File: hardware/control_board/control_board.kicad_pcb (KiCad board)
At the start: 2 copper layers, 101.6 x 53.3 mm, 38 parts, among them J1 PWR_SWITCHES, J10 MO2_SW_FW, J11 MO3_SW_FW, J12 MO0_SW_BW, J13 MO1_SW_BW, J14 MO2_SW_BW, J15 MO3_SW_BW, J2 UI_SWITCHES, J3 ATX-24, J4 MOT0, J5 MOT1, J6 MOT2, J7 MOT3, J8 MO0_SW_FW, J9 MO1_SW_FW, P1 Digital, P2 Power, P3 Analog, P4 Analog, P5 PWM, P6 PWM, P7 Communication, Q1 BSS138

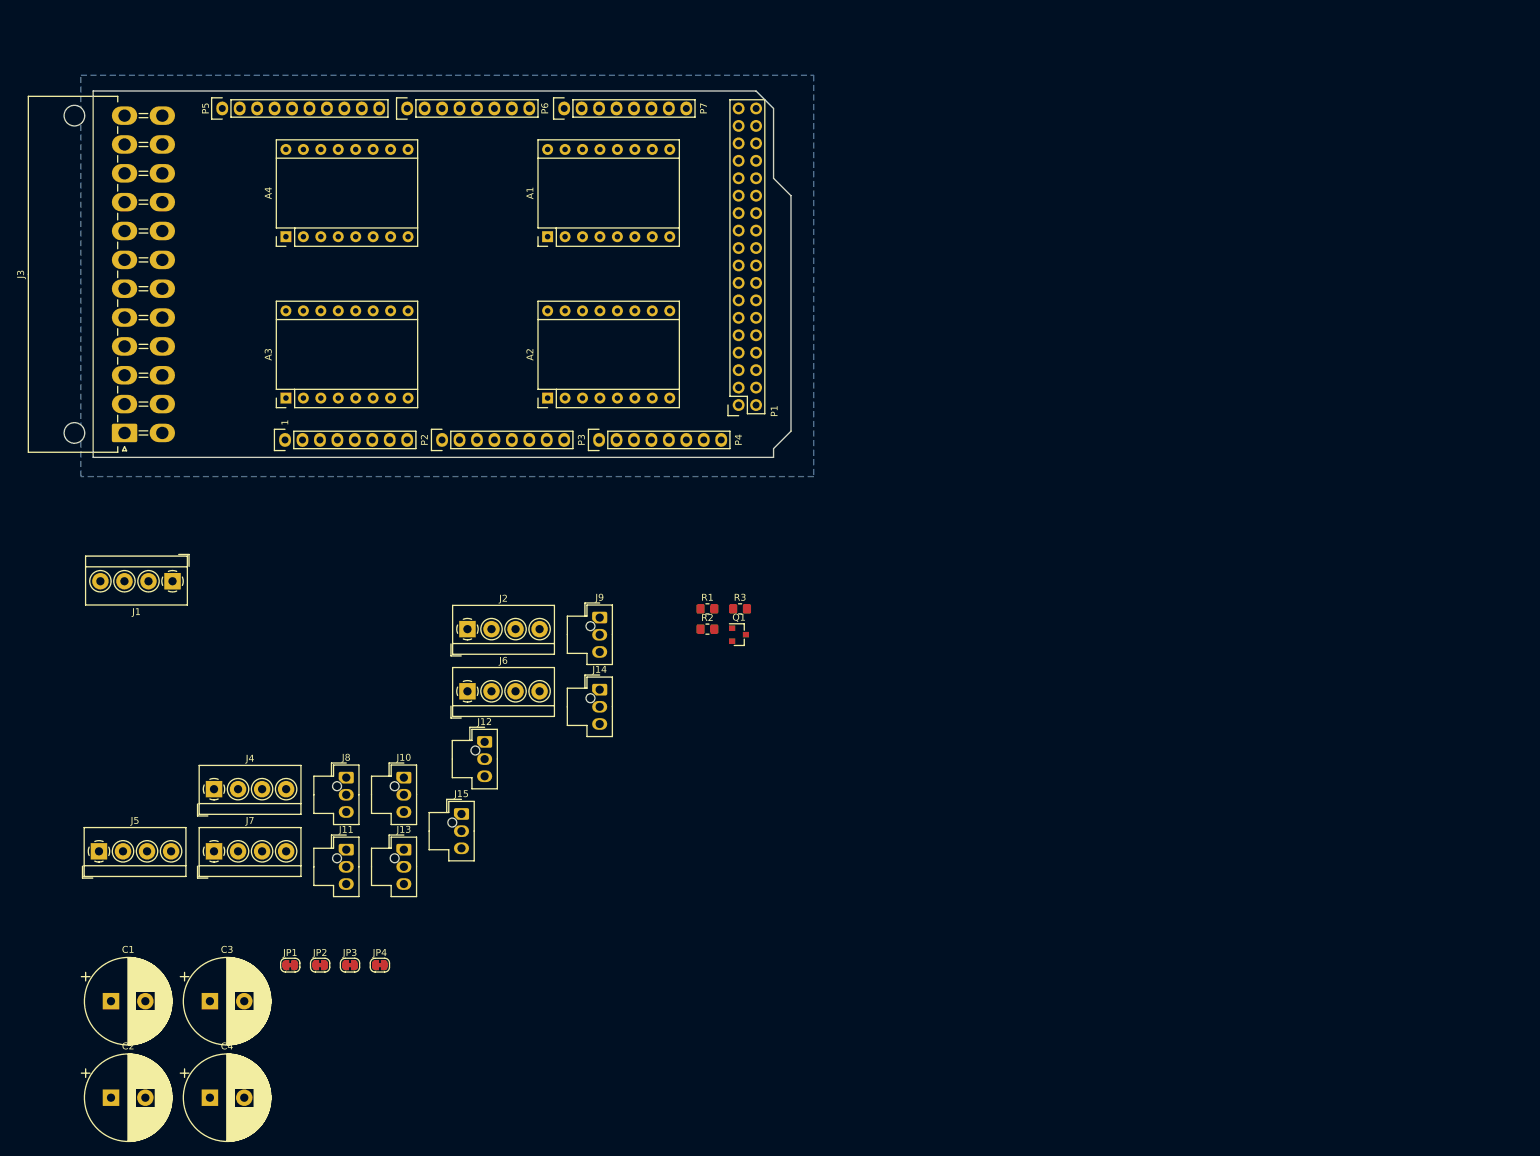
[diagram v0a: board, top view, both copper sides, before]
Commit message: add ps on led
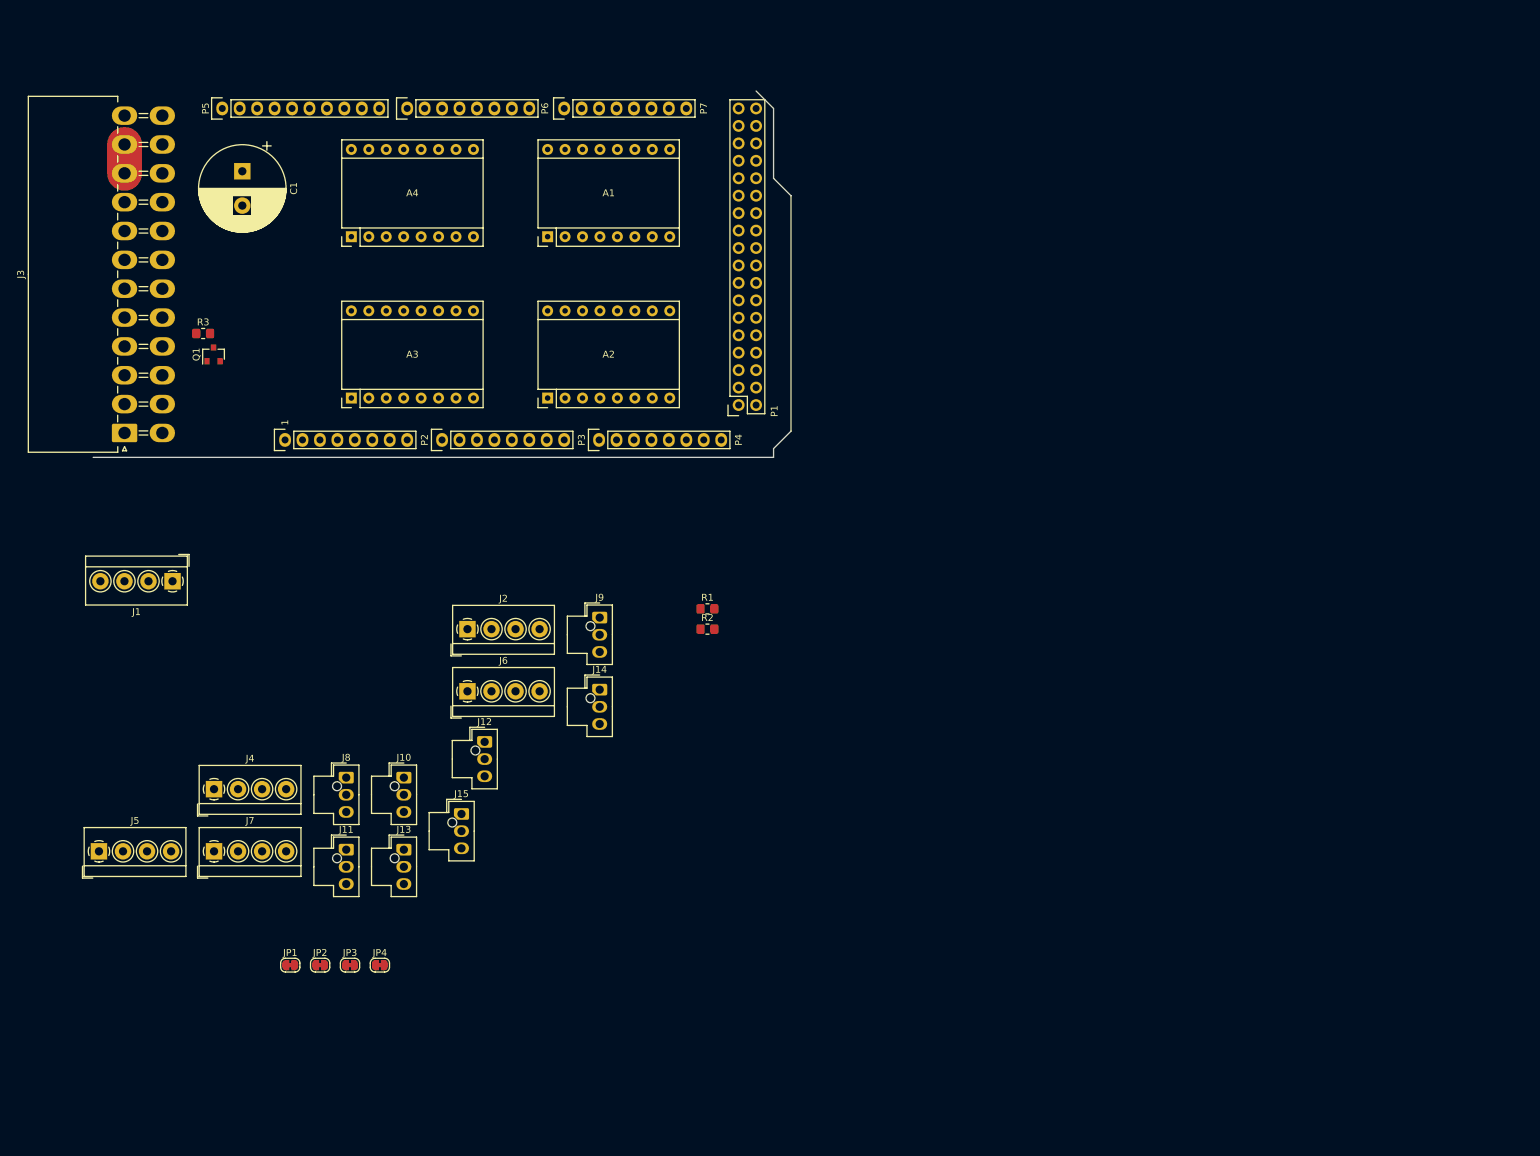
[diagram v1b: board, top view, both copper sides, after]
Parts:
- removed C2, C3, C4: 100uF, Capacitor_THT:CP_Radial_D12.5mm_P5.00mm
- moved C1 122.3 mm to (125.1, 80.0), turned to 270 degrees
- moved R3 87.9 mm to (119.4, 103.6)
- moved Q1 86.7 mm to (120.9, 106.7), turned to 90 degrees
- moved A3 9.53 mm to (141.0, 113.0)
- moved A4 9.53 mm to (141.0, 89.5)
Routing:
- net +12V: track 0.00 -> 4.20 mm
- added copper zone on In1.Cu, net PWR_SW_L
- removed copper zone on B.Cu, net PWR_SW_L
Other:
- outline, holes or cut-outs redrawn
- copper layers 2 -> 4
- rule trace_min: 0.2 -> 0.1524

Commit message: add misc connectors
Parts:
- added D1: PS_ON, LED_SMD:LED_0805_2012Metric_Pad1.15x1.40mm_HandSolder, F.Cu at (305.7, 108.7)
- added J16: MISC_SIG, TerminalBlock_4Ucon:TerminalBlock_4Ucon_1x04_P3.50mm_Horizontal, F.Cu at (232.7, 138.8)
- added J17: MISC_PWR, TerminalBlock_4Ucon:TerminalBlock_4Ucon_1x04_P3.50mm_Horizontal, F.Cu at (249.5, 129.7)
- added R4: R_200, Resistor_SMD:R_0805_2012Metric_Pad1.20x1.40mm_HandSolder, F.Cu at (310.4, 111.7)
- moved J13 160.8 mm to (293.9, 109.9)
- moved J7 160.1 mm to (266.2, 111.6)
- moved J4 141.2 mm to (249.5, 111.6)
- moved J11 137.7 mm to (268.7, 129.5)
- moved J8 137.7 mm to (268.7, 119.0)
- moved J5 137.7 mm to (232.7, 129.7)
- moved C1 133.8 mm to (234.5, 157.0), turned to 0 degrees
- moved J15 127.5 mm to (277.1, 130.9)
- moved J12 124.3 mm to (277.1, 120.4)
- moved R2 123.6 mm to (310.4, 108.7)
- moved JP1 122.3 mm to (246.2, 151.7)
- moved J1 121.1 mm to (232.7, 111.6), turned to 0 degrees
- moved JP3 118.2 mm to (250.5, 151.7)
- moved R1 117.3 mm to (305.6, 111.7)
- moved JP2 116.9 mm to (246.2, 155.3)
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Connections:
- P1 pad 10: /Arduino Shield Connections/47 -> MISC_1
- P1 pad 7: /Arduino Shield Connections/48 -> MISC_2
- P1 pad 8: /Arduino Shield Connections/49 -> MISC_3
- P1 pad 9: /Arduino Shield Connections/46 -> MISC_0
- P5 pad 5: /Arduino Shield Connections/13(**) -> UI_SWITCH_1
- P5 pad 6: /Arduino Shield Connections/12(**) -> UI_SWITCH_0

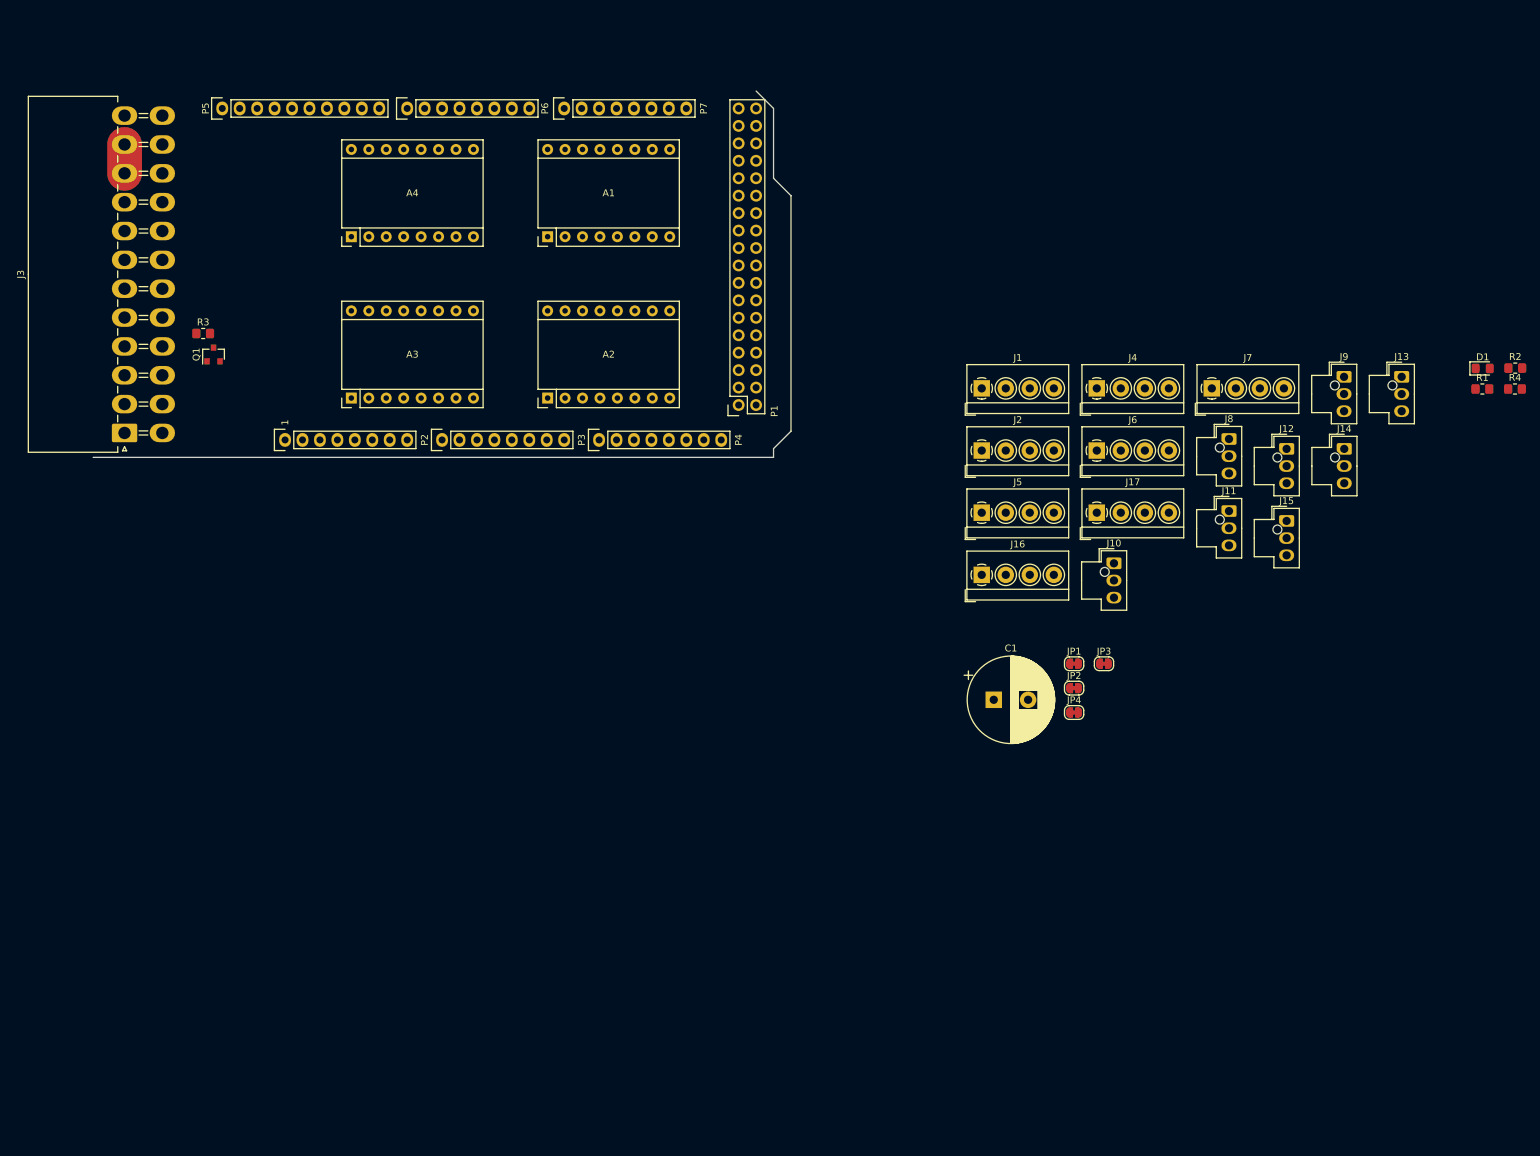
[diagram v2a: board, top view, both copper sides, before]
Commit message: finish layout, add fusing
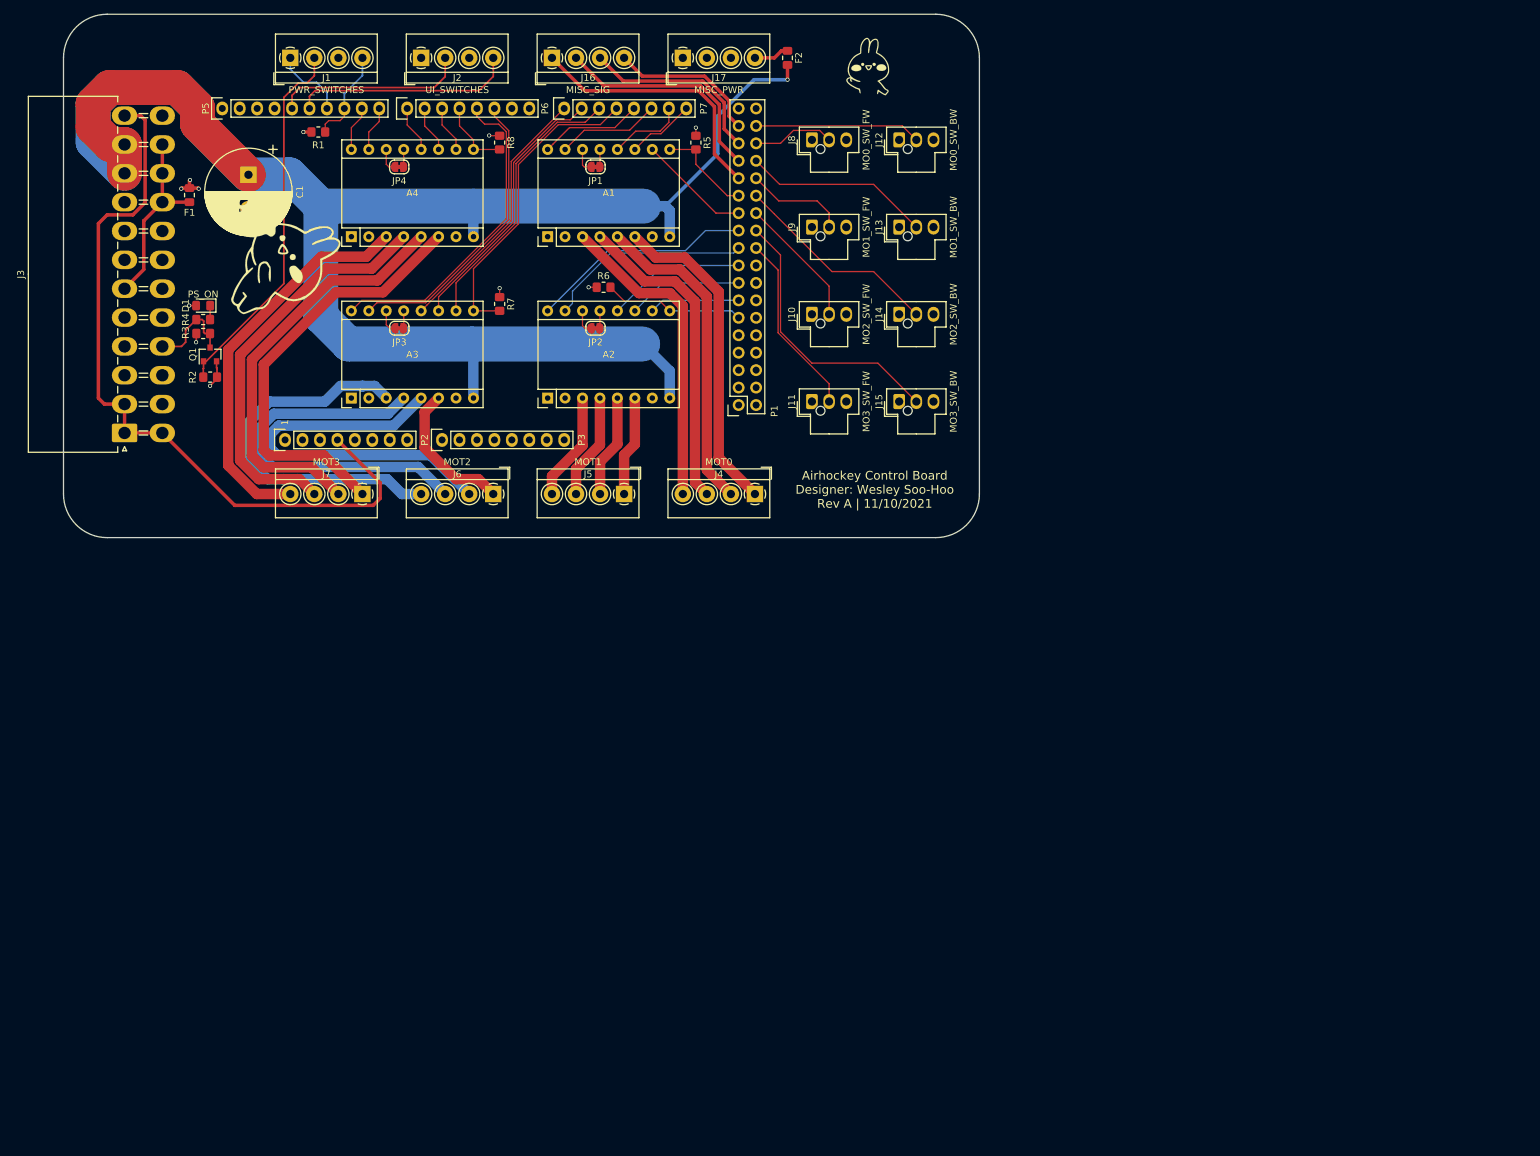
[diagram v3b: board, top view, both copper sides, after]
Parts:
- removed P4: Analog, Socket_Arduino_Mega:Socket_Strip_Arduino_1x08
- added F1: 1A, Fuse:Fuse_0805_2012Metric_Pad1.15x1.40mm_HandSolder, F.Cu at (117.4, 83.5)
- added F2: 1A, Fuse:Fuse_0805_2012Metric_Pad1.15x1.40mm_HandSolder, F.Cu at (204.5, 63.5)
- added G***: LOGO, img:mimi_doll, B.Cu at (188.0, 94.0)
- added G***: LOGO, img:mimi_heart, F.Cu at (128.9, 91.4)
- added G***: LOGO, img:mimi, F.Cu at (216.5, 64.1)
- added G***: LOGO, img:mimi_melon, B.Cu at (132.1, 111.8)
- added R5: R_10K, Resistor_SMD:R_0805_2012Metric_Pad1.20x1.40mm_HandSolder, F.Cu at (191.1, 75.8)
- added R6: R_10K, Resistor_SMD:R_0805_2012Metric_Pad1.20x1.40mm_HandSolder, F.Cu at (177.7, 96.9)
- added R7: R_10K, Resistor_SMD:R_0805_2012Metric_Pad1.20x1.40mm_HandSolder, F.Cu at (162.6, 99.3)
- added R8: R_10K, Resistor_SMD:R_0805_2012Metric_Pad1.20x1.40mm_HandSolder, F.Cu at (162.6, 75.8)
- moved R4 191.3 mm to (119.4, 101.6), turned to 180 degrees
- moved R2 190.0 mm to (120.4, 110.0)
- moved D1 186.5 mm to (119.4, 99.6), turned to 180 degrees
- moved R1 173.6 mm to (136.2, 74.3)
- moved C1 132.7 mm to (126.0, 80.5), turned to 270 degrees
- moved JP4 126.4 mm to (147.9, 79.4)
- moved J7 124.6 mm to (142.6, 127.0), turned to 180 degrees
- moved JP3 113.6 mm to (148.0, 102.9)
- moved J1 111.6 mm to (132.1, 63.5)
- moved JP1 100.4 mm to (176.5, 79.4)
- moved J2 99.7 mm to (151.1, 63.5)
- moved J16 97.9 mm to (170.2, 63.5)
- moved J17 89.5 mm to (189.2, 63.5)
- moved J6 88.1 mm to (161.6, 127.0), turned to 180 degrees
- moved JP2 87.2 mm to (176.5, 102.9)
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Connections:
- net /Connectors/5V_SB renamed Net-(J3-Pad9)
- J17 pad 4: +12V -> Net-(F2-Pad1)
- J2 pad 2: UI_SWITCH_0 -> UI_SWITCH_1
- J2 pad 4: UI_SWITCH_1 -> UI_SWITCH_0
- J3 pad 21: +5V -> /Connectors/5VPS
- J3 pad 22: +5V -> /Connectors/5VPS
- J3 pad 23: +5V -> /Connectors/5VPS
- J3 pad 4: +5V -> /Connectors/5VPS
- J3 pad 6: +5V -> /Connectors/5VPS
- P1 pad 10: MISC_1 -> /Arduino Shield Connections/47
- P1 pad 11: MOT1_MS3 -> ~MOT1_EN
- P1 pad 12: ~MOT3_EN -> /Arduino Shield Connections/45
- P1 pad 13: MOT1_MS2 -> MOT1_MS1
- P1 pad 14: MOT3_STEP -> /Arduino Shield Connections/43
- P1 pad 15: MOT1_MS1 -> MOT1_MS2
- P1 pad 16: MOT3_DIR -> /Arduino Shield Connections/41
- P1 pad 17: MOT1_DIR -> MOT1_MS3
- P1 pad 18: MOT3_MS1 -> /Arduino Shield Connections/39
- P1 pad 20: MOT3_MS2 -> MOT3_SWITCH_FW
- P1 pad 21: ~MOT1_EN -> MOT1_DIR
- P1 pad 22: MOT3_MS3 -> MOT3_SWITCH_BW
- P1 pad 23: MOT0_MS3 -> MOT0_MS1
- P1 pad 24: ~MOT2_EN -> MOT2_SWITCH_FW
- P1 pad 25: MOT0_MS2 -> ~MOT0_EN
- P1 pad 26: MOT2_STEP -> MOT2_SWITCH_BW
- P1 pad 27: MOT0_MS1 -> MISC_0
- P1 pad 28: MOT2_DIR -> MOT1_SWITCH_FW
- P1 pad 29: MOT0_DIR -> MISC_1
- P1 pad 30: MOT2_MS1 -> MOT1_SWITCH_BW
- P1 pad 31: MOT0_STEP -> MISC_2
- P1 pad 32: MOT2_MS2 -> MOT0_SWITCH_FW
- P1 pad 33: ~MOT0_EN -> MISC_3
- P1 pad 34: MOT2_MS3 -> MOT0_SWITCH_BW
- P1 pad 7: MISC_2 -> /Arduino Shield Connections/48
- P1 pad 8: MISC_3 -> /Arduino Shield Connections/49
- P1 pad 9: MISC_0 -> /Arduino Shield Connections/46
- P5 pad 10: MOT3_SWITCH_FW -> MOT3_STEP
- P5 pad 9: MOT3_SWITCH_BW -> MOT3_DIR
- P6 pad 1: MOT2_SWITCH_BW -> MOT3_MS3
- P6 pad 2: MOT2_SWITCH_FW -> MOT3_MS2
- P6 pad 3: MOT1_SWITCH_BW -> MOT3_MS1
- P6 pad 4: MOT1_SWITCH_FW -> ~MOT3_EN
- P6 pad 5: MOT0_SWITCH_BW -> MOT2_DIR
- P6 pad 6: MOT0_SWITCH_FW -> MOT2_STEP
- P7 pad 1: /Arduino Shield Connections/14(Tx3) -> MOT2_MS3
- P7 pad 2: /Arduino Shield Connections/15(Rx3) -> MOT2_MS2
- P7 pad 3: /Arduino Shield Connections/16(Tx2) -> MOT2_MS1
- P7 pad 4: /Arduino Shield Connections/17(Rx2) -> ~MOT2_EN
- P7 pad 5: /Arduino Shield Connections/18(Tx1) -> MOT0_DIR
- P7 pad 6: /Arduino Shield Connections/19(Rx1) -> MOT0_STEP
- P7 pad 7: /Arduino Shield Connections/20(SDA) -> MOT0_MS3
- P7 pad 8: /Arduino Shield Connections/21(SCL) -> MOT0_MS2
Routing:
- net +12V: track 4.20 -> 270.3 mm, vias 0 -> 1
- net +3V3: track 0.00 -> 110.2 mm
- net MOT3_2B: track 0.00 -> 62.6 mm
- net MOT3_2A: track 0.00 -> 60.9 mm
- net MOT3_1A: track 0.00 -> 59.2 mm
- net MOT2_2A: track 0.00 -> 57.9 mm
- net MOT3_1B: track 0.00 -> 57.4 mm
- net MOT2_1A: track 0.00 -> 56.2 mm
- net MOT2_1B: track 0.00 -> 56.0 mm
- net ESTOP_H: track 0.00 -> 54.2 mm
- net MOT0_2B: track 0.00 -> 47.2 mm
- net MOT2_DIR: track 0.00 -> 47.1 mm
- net MOT0_2A: track 0.00 -> 46.8 mm
- net MOT0_1A: track 0.00 -> 46.5 mm
- net MOT0_1B: track 0.00 -> 46.2 mm
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- added copper zone on In2.Cu, net +5V
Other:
- board size 101.6 x 53.3 mm -> 133.3 x 76.2 mm
- board text added: "Airhockey Control Board Designer: Wesley Soo-Hoo Rev A | 11/10/2021"
